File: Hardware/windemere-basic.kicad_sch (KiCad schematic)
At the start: 66 parts, among them J1 A_40-LC-TT, J2 A_40-LC-TT, J3 Connector, J4 A_28-LC-TT, J5 A_28-LC-TT, J6 Barrel_Jack, SW1 Reset Button, U1 HD44780U, U2 WD65C02, U3 28C256, U4 62256, U5 WD65C22, U6 74HC00, U7 MM74C922, U8 L7805, U9 MCP102-475, X1 1MHz

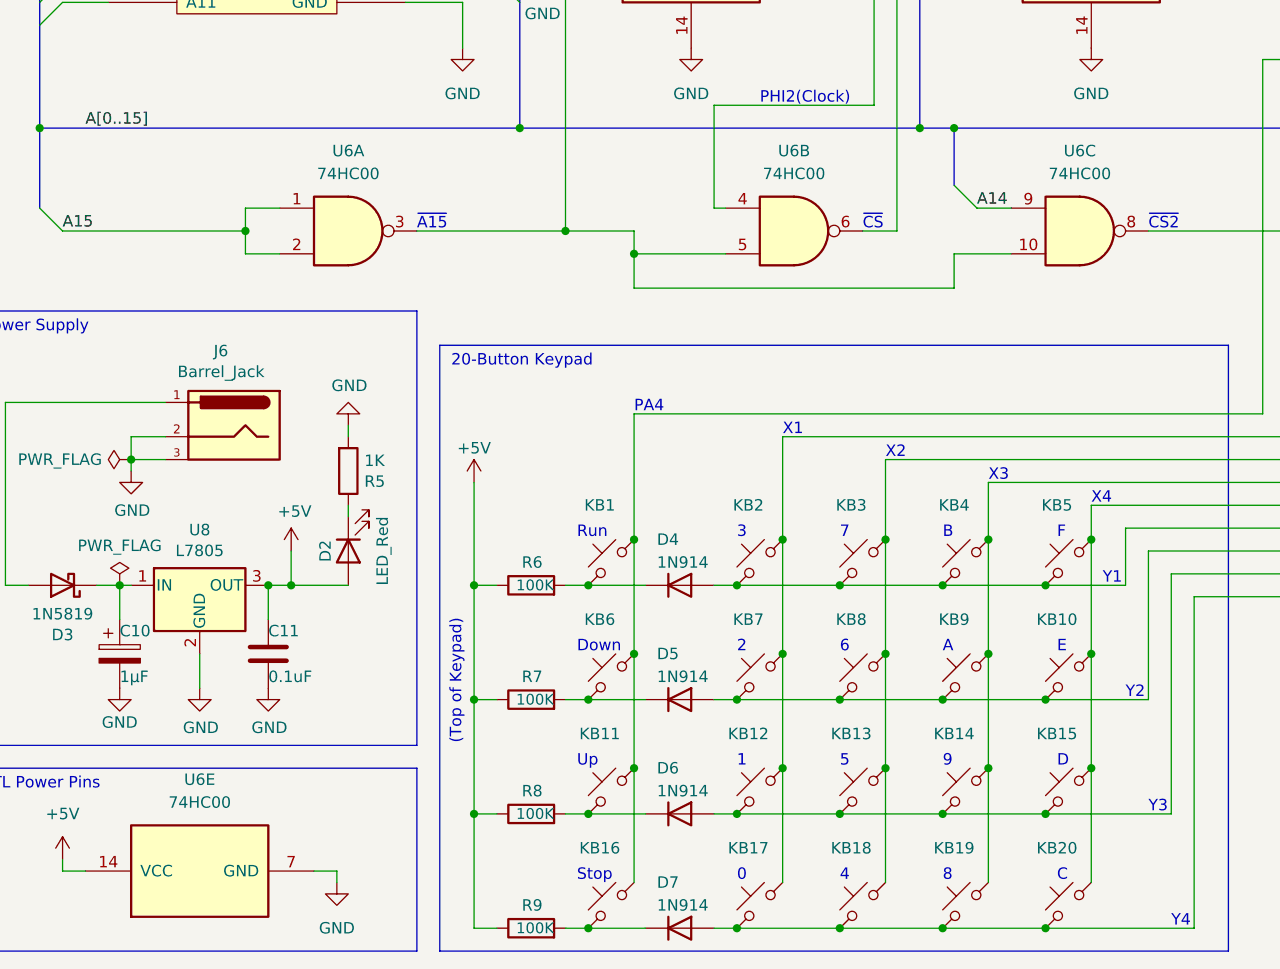
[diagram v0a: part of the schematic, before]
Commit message: Hardware: Change from 74HC00 to 74LS00
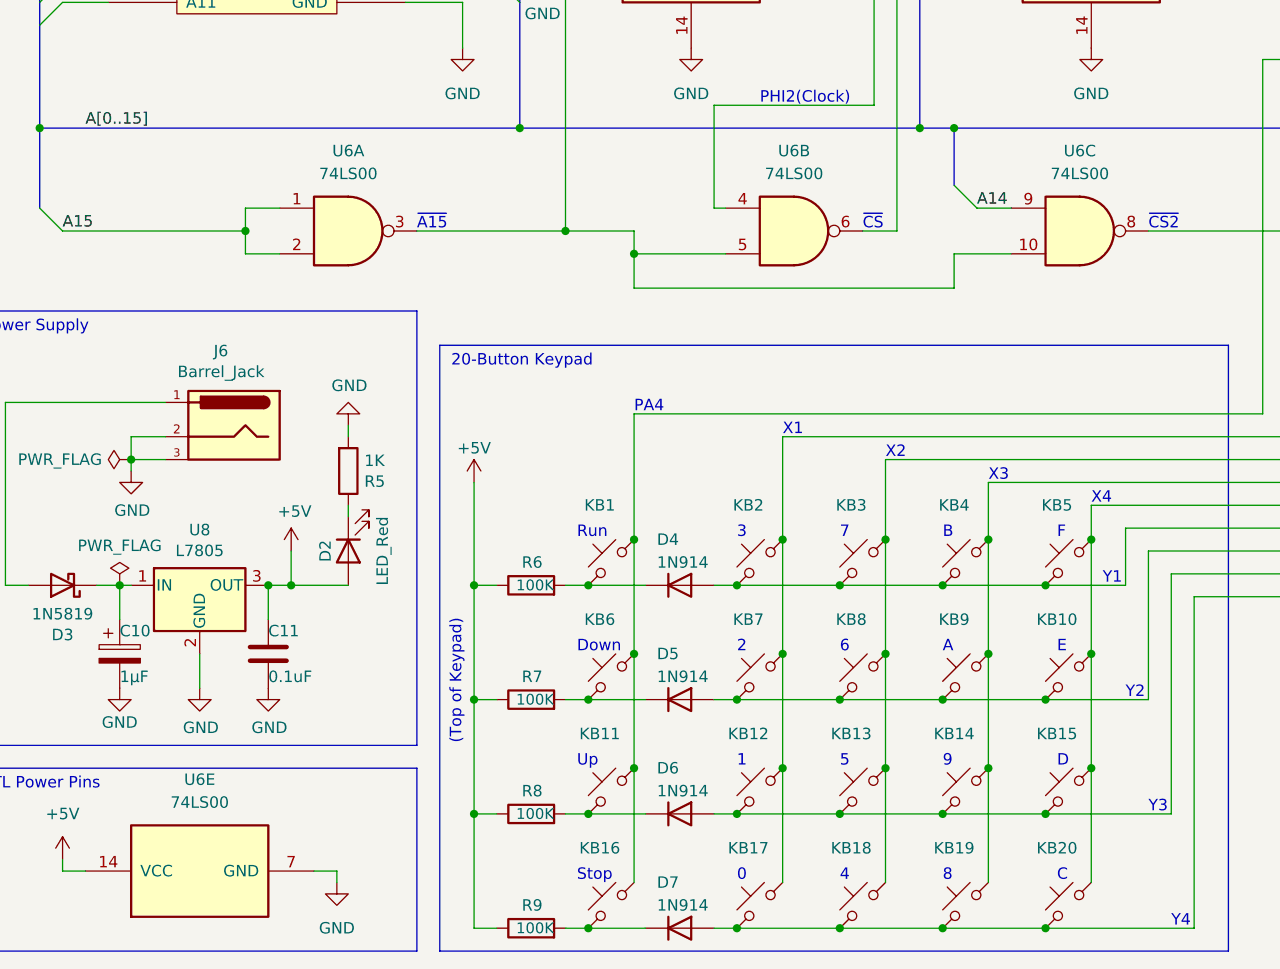
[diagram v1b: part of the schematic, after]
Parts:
- U6: value 74HC00 -> 74LS00
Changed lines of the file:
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@@
       (effects (font (size 1.27 1.27)))
     )
-    (property "Value" "74HC00" (at 106.68 115.57 0)
+    (property "Value" "74LS00" (at 106.68 115.57 0)
       (effects (font (size 1.27 1.27)))
     )
@@
       (effects (font (size 1.27 1.27)) hide)
     )
-    (property "Datasheet" "http://www.ti.com/lit/gpn/sn74hc00" (at 106.68 121.92 0)
+    (property "Datasheet" "https://www.ti.com/lit/gpn/sn74ls00" (at 106.68 121.92 0)
       (effects (font (size 1.27 1.27)) hide)
     )
@@
       (effects (font (size 1.27 1.27)))
     )
-    (property "Value" "74HC00" (at 40.64 185.42 90)
+    (property "Value" "74LS00" (at 40.64 185.42 90)
       (effects (font (size 1.27 1.27)))
     )
@@
       (effects (font (size 1.27 1.27)) hide)
     )
-    (property "Datasheet" "http://www.ti.com/lit/gpn/sn74hc00" (at 40.64 193.04 0)
+    (property "Datasheet" "https://www.ti.com/lit/gpn/sn74ls00" (at 40.64 193.04 0)
       (effects (font (size 1.27 1.27)) hide)
     )
@@
       (effects (font (size 1.27 1.27)))
     )
-    (property "Value" "74HC00" (at 138.43 115.57 0)
+    (property "Value" "74LS00" (at 138.43 115.57 0)
       (effects (font (size 1.27 1.27)))
     )
@@
       (effects (font (size 1.27 1.27)) hide)
     )
-    (property "Datasheet" "http://www.ti.com/lit/gpn/sn74hc00" (at 138.43 121.92 0)
+    (property "Datasheet" "https://www.ti.com/lit/gpn/sn74ls00" (at 138.43 121.92 0)
       (effects (font (size 1.27 1.27)) hide)
     )
@@
       (effects (font (size 1.27 1.27)))
     )
-    (property "Value" "74HC00" (at 57.15 115.57 0)
+    (property "Value" "74LS00" (at 57.15 115.57 0)
       (effects (font (size 1.27 1.27)))
     )
@@
       (effects (font (size 1.27 1.27)) hide)
     )
-    (property "Datasheet" "http://www.ti.com/lit/gpn/sn74hc00" (at 57.15 121.92 0)
-      (effects (font (size 1.27 1.27)) hide)
-    )
+    (property "Datasheet" "https://www.ti.com/lit/gpn/sn74ls00" (at 57.15 121.92 0)
+      (effects (font (size 1.27 1.27)) hide)
+    )

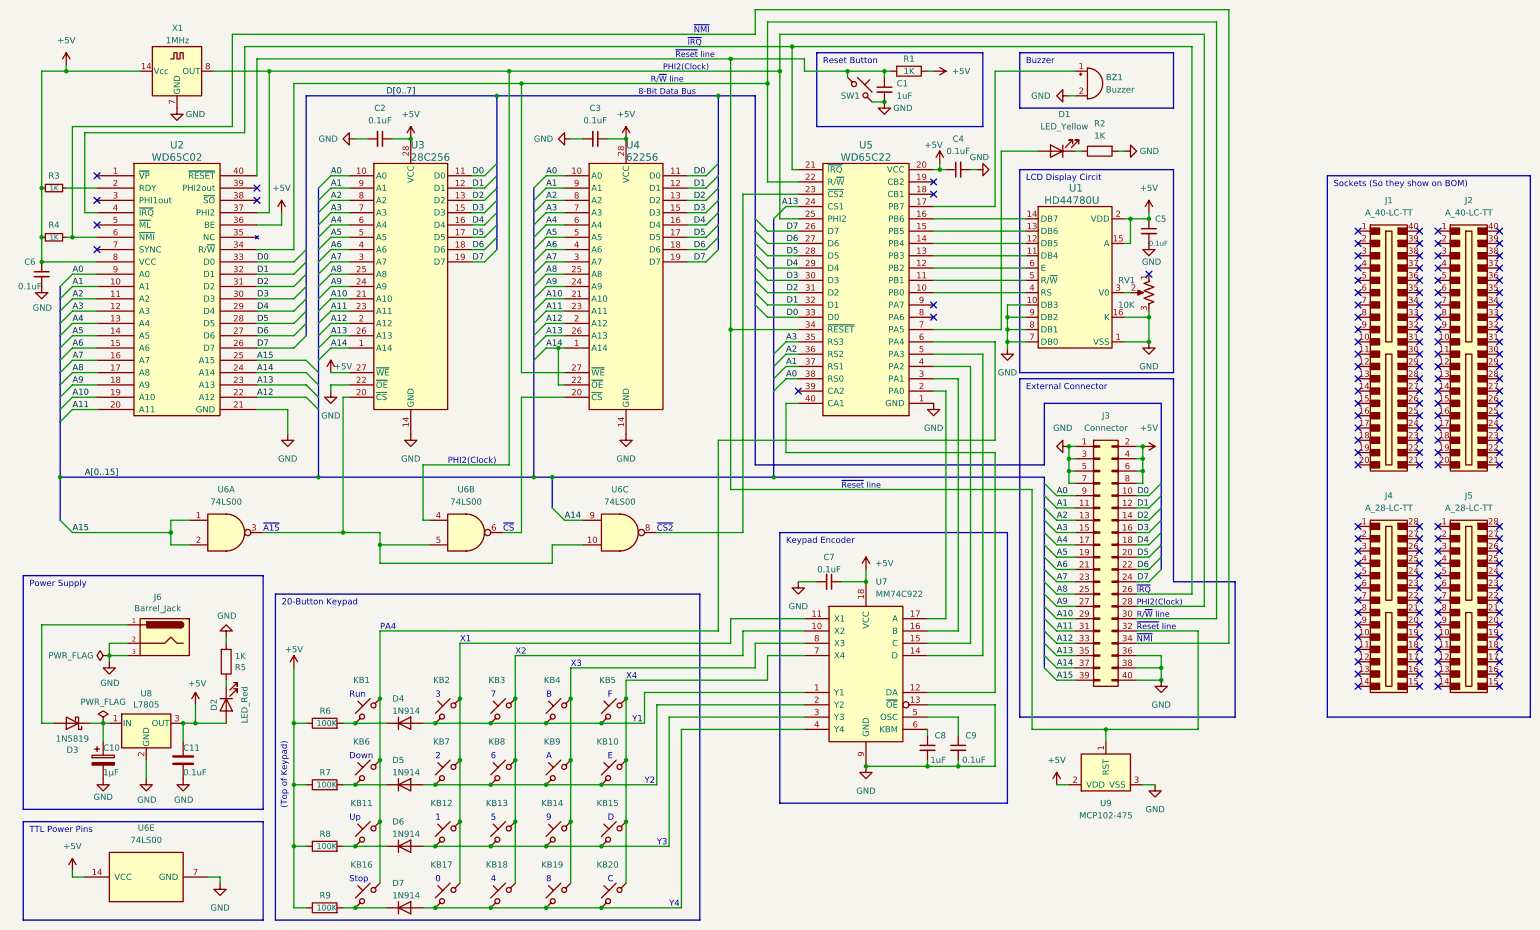
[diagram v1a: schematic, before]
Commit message: Change to MM74LS923
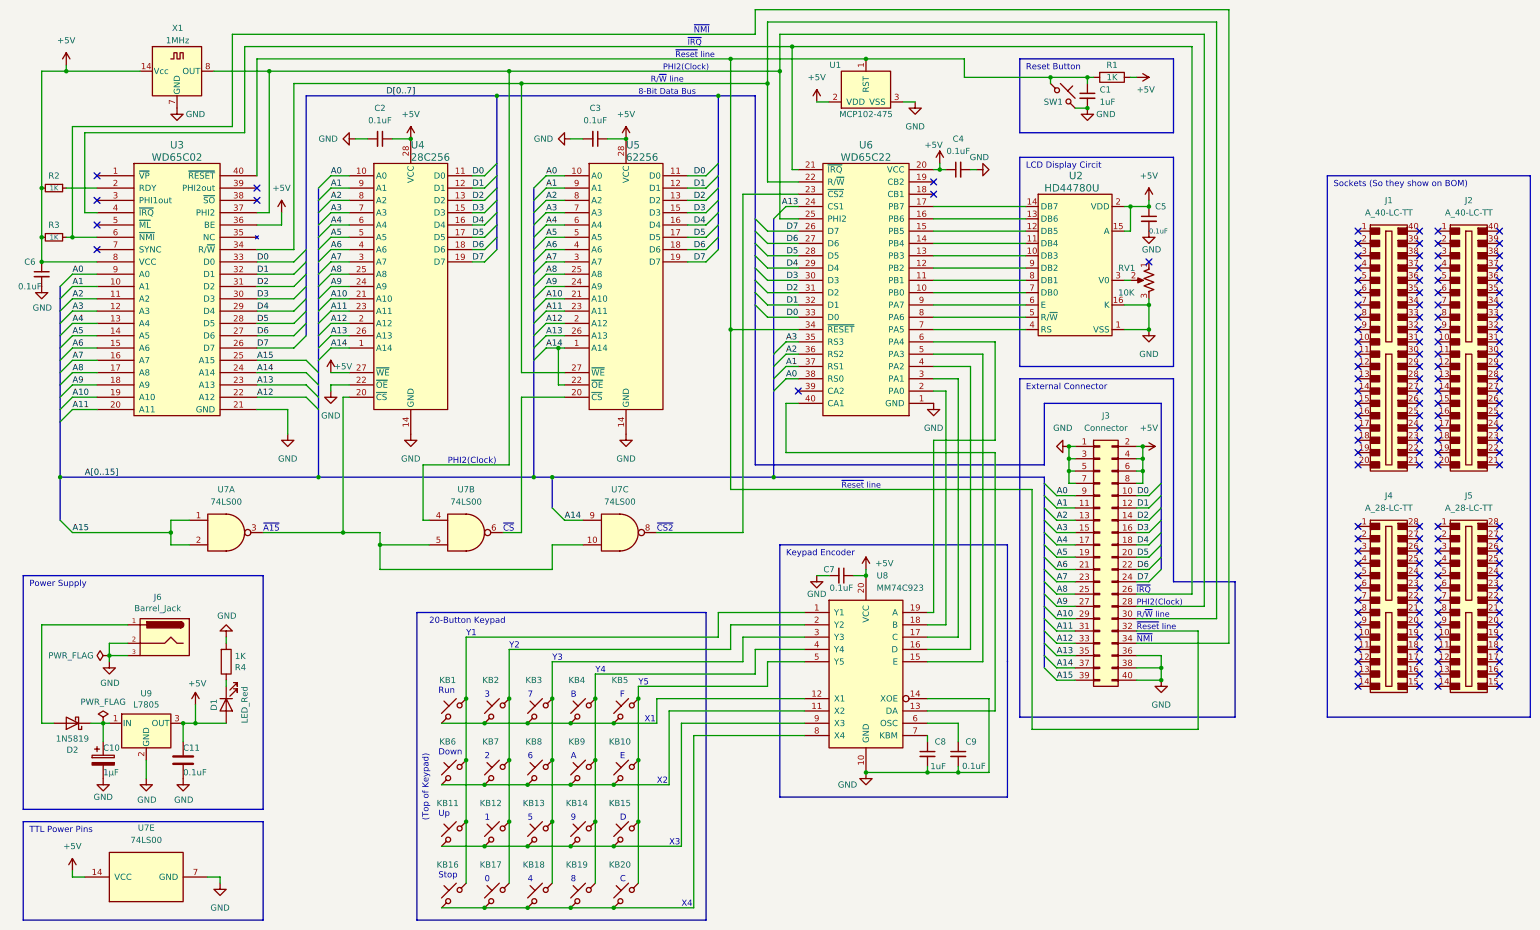
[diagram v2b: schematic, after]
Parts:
- removed BZ1: Buzzer, Buzzer_Beeper:Buzzer_12x9.5RM7.6, symbol Device:Buzzer
- removed D1: LED_Yellow, LED_THT:LED_D5.0mm, symbol Device:LED
- removed D4, D5, D6, D7: 1N914, Diode_THT:D_DO-35_SOD27_P7.62mm_Horizontal, symbol Diode:1N914
- removed R2: 1K, Resistor_THT:R_Axial_DIN0207_L6.3mm_D2.5mm_P10.16mm_Horizontal, symbol Device:R
- removed R6, R7, R8, R9: 100K, Resistor_THT:R_Axial_DIN0207_L6.3mm_D2.5mm_P10.16mm_Horizontal, symbol Device:R
- removed U9: MCP102-475, Package_TO_SOT_THT:TO-92, symbol Power_Supervisor:MCP101-475D
- added U1: MCP102-475, Package_TO_SOT_THT:TO-92, symbol Power_Supervisor:MCP101-475D
- J3: footprint Connector_PinHeader_2.54mm:PinHeader_2x20_P2.54mm_Vertical -> Connector_PCBEdge:Samtec_MECF-20-0_-NP-L-DV_2x20_P1.27mm_Edge
- U8: renamed from U7; value MM74C922 -> MM74C923; symbol 74xx:MM74C922 -> 74xx:MM74C923
- renumbered D2 to D1, D3 to D2, R3 to R2, R4 to R3, R5 to R4, U1 to U2, U2 to U3, U3 to U4, U4 to U5, U5 to U6, U6 to U7, U8 to U9
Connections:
- net +5V: now also U8.20 (VCC), U1.2 (VDD); no longer U8.18 (VCC)
- net GND: now also U8.10 (GND), U8.14 (XOE), U1.3 (VSS); no longer U2.10 (DB3), U2.7 (DB0), U2.8 (DB1), U2.9 (DB2), U8.13 (~{OE}), U8.9 (GND)
- net at KB1.1: now also KB2.1, KB3.1, KB4.1, KB5.1, U8.12 (X1)
- net at U6.17 (PB7): now also U2.14 (DB7)
- net at KB6.1: now also KB10.1, KB7.1, KB8.1, KB9.1, U8.11 (X2)
- net at C9.1: now also U8.6 (OSC); no longer U8.5 (OSC)
- net at C1.1, J3.32 (Pin_32), R1.2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: now also U1.1 (RST)
- net at KB17.1, KB18.1, KB19.1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: now also KB16.1, U8.8 (X4); no longer U8.4 (Y4)
- net at KB10.2, KB15.2, KB20.2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: now also U8.5 (Y5); no longer U8.7 (X4)
- net at KB12.1, KB13.1, KB14.1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: now also KB11.1, U8.9 (X3); no longer U8.3 (Y3)
- net at KB13.2, KB18.2, KB3.2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: now also U8.3 (Y3); no longer U8.10 (X2)
- net at KB14.2, KB19.2, KB4.2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: now also U8.4 (Y4); no longer U8.8 (X3)
- net at KB1.2, KB11.2, KB16.2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: now also U8.1 (Y1); no longer U6.6 (PA4)
- net at U6.7 (PA5): now also U2.4 (RS)
- net at KB12.2, KB17.2, KB2.2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: now also U8.2 (Y2); no longer U8.11 (X1)
- net at U6.10 (PB0): now also U2.7 (DB0); no longer U2.4 (RS)
- net at U6.11 (PB1): now also U2.8 (DB1); no longer U2.5 (R/~{W})
- net at U6.12 (PB2): now also U2.9 (DB2); no longer U2.6 (E)
- net at U6.13 (PB3): now also U2.10 (DB3); no longer U2.11 (DB4)
- net at U6.14 (PB4): now also U2.11 (DB4); no longer U2.12 (DB5)
- net at U6.15 (PB5): now also U2.12 (DB5); no longer U2.13 (DB6)
- net at U6.16 (PB6): now also U2.13 (DB6); no longer U2.14 (DB7)
- net at U6.2 (PA0): now also U8.18 (B); no longer U8.17 (A)
- net at U6.3 (PA1): now also U8.17 (C); no longer U8.16 (B)
- net at U6.4 (PA2): now also U8.16 (D); no longer U8.15 (C)
- net at U6.40 (CA1): now also U8.13 (DA); no longer U8.12 (DA)
- net at U6.5 (PA3): now also U8.15 (E); no longer U8.14 (D)
- net at U6.8 (PA6): now also U2.5 (R/~{W})
- net at U6.9 (PA7): now also U2.6 (E)
- net at C8.1: now also U8.7 (KBM); no longer U8.6 (KBM)
- new net: U6.6 (PA4), U8.19 (A)
- no-connect marks 148 -> 146
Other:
- note added: "Y5"
- note removed: "Buzzer"
- note removed: "PA4"
- moved on the sheet: C1, C5, C7, C8, C9, KB1, KB10, KB11, KB12, KB13, KB14, KB15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
